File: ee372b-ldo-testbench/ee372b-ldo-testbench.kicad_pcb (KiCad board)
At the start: 4 copper layers, 100 x 100 mm, 128 parts, among them J1 PEC02SAAN, J10 OUT_S, J11 VOUT, J12 VDD_BUF, J13 V_SIG, J14 PEC03SAAN, J15 VSIG_BUF, J16 PEC03SAAN, J17 PEC03SAAN, J18 PEC03SAAN, J19 PEC03SAAN, J2 PEC02SAAN, J20 VREF_EXTERNAL, J21 PEC02SAAN, J22 PEC02SAAN, J23 PEC02SAAN, J24 PEC02SAAN, J25 PEC03SAAN, J3 GND, J4 1V8, J5 3v3_EXTERNAL, J6 GND, J9 IN_S, Q1 FDV305N, Q2 FDV305N, Q3 FDV305N, Q4 FDV305N, Q5 FDV305N, U1 MMSZ4679T1G, U3 ADS1220IPW, U4 BUF634AIDR

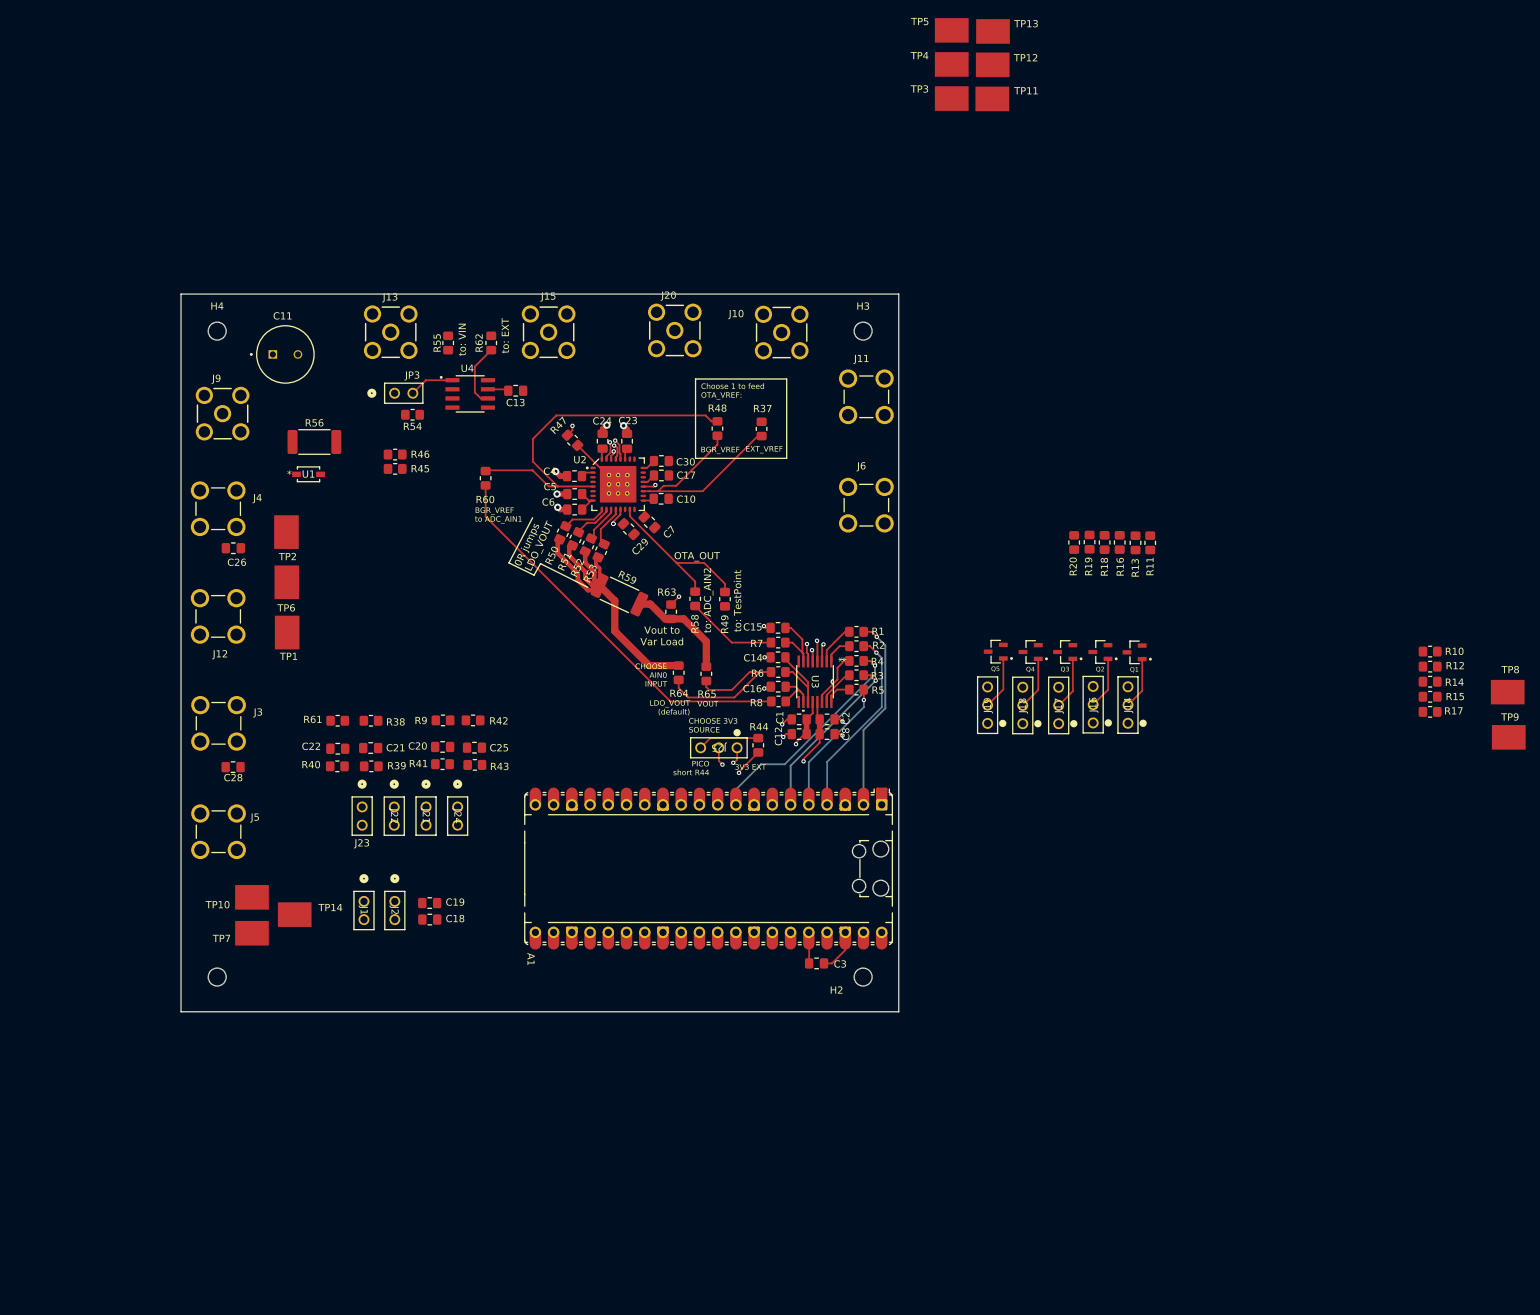
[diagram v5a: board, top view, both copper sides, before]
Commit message: resistor bank wired
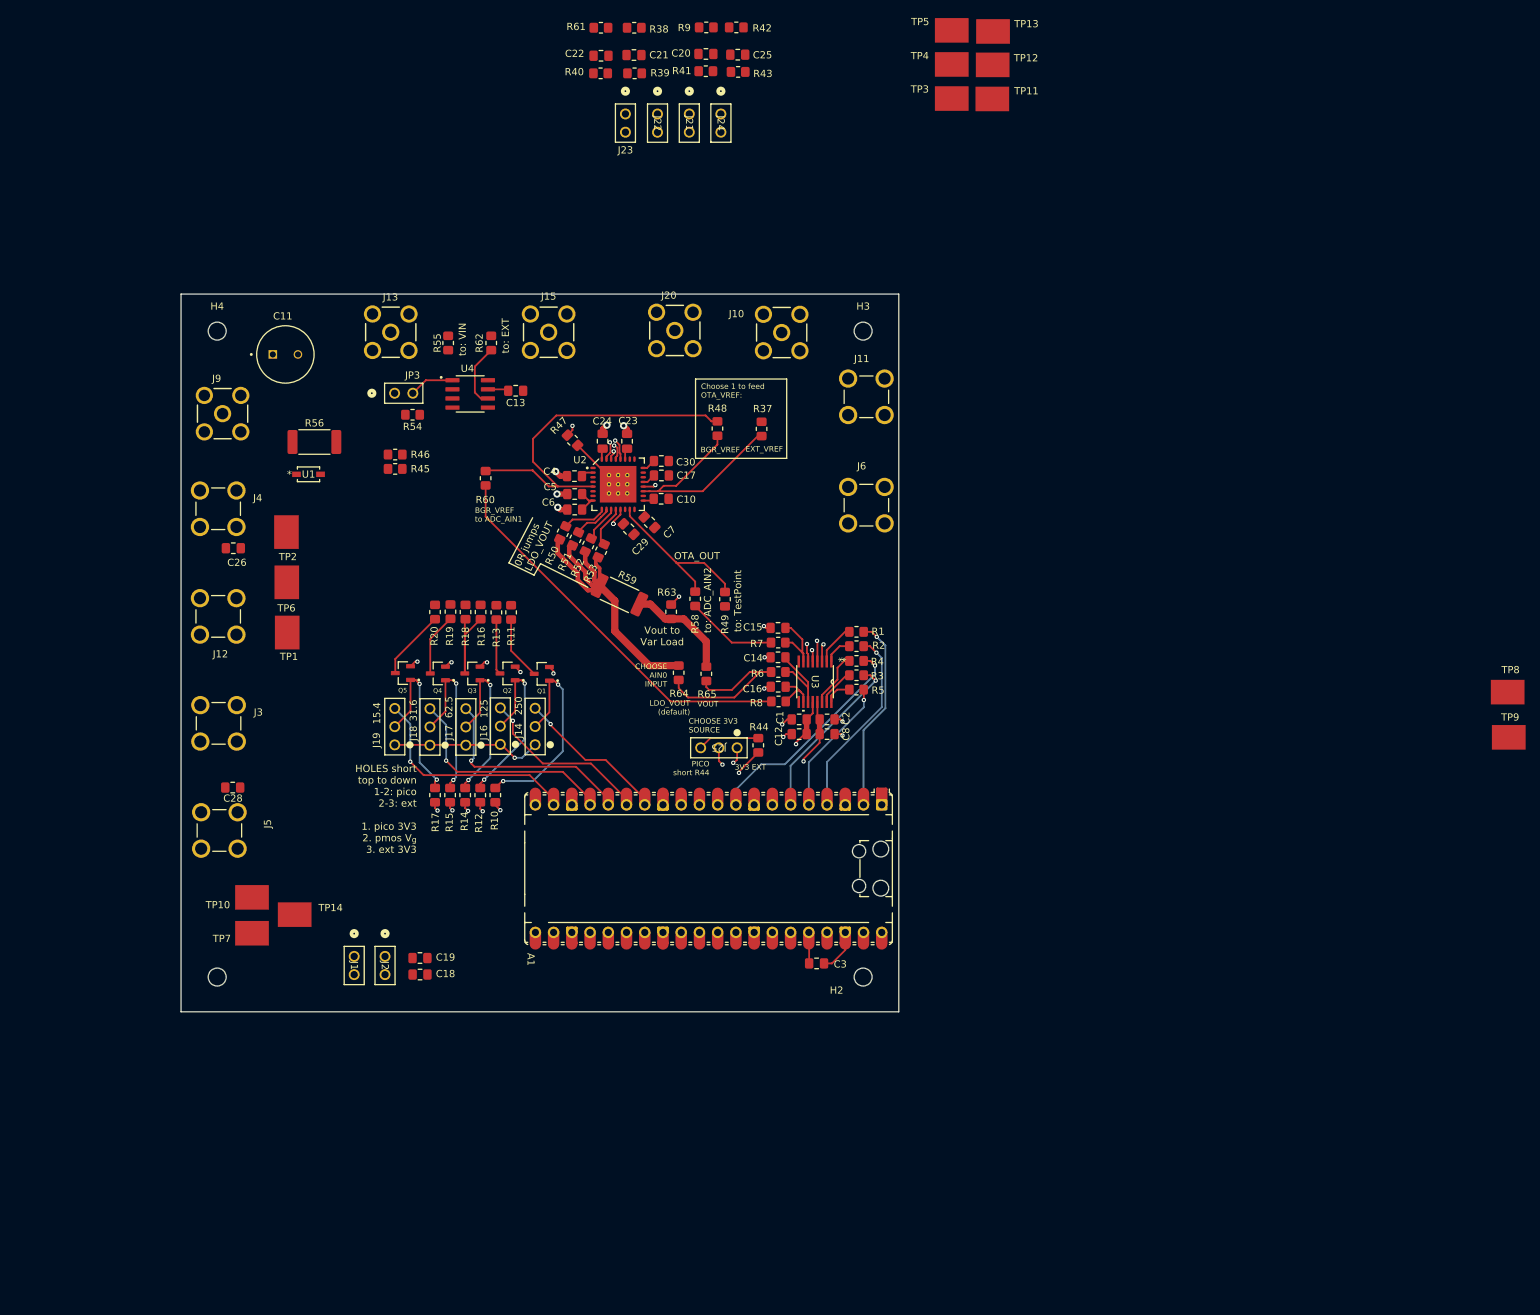
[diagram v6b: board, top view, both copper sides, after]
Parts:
- moved R17 139.1 mm to (175.3, 86.7), turned to -90 degrees
- moved R15 137.2 mm to (177.4, 86.7), turned to -90 degrees
- moved R14 135.4 mm to (179.6, 86.7), turned to -90 degrees
- moved R12 133.6 mm to (181.7, 86.7), turned to -90 degrees
- moved R10 131.8 mm to (183.8, 86.7), turned to -90 degrees
- moved C21 103.3 mm to (203.1, -16.5)
- moved C25 103.3 mm to (217.5, -16.5)
- moved R61 103.3 mm to (198.5, -20.3)
- moved C20 103.3 mm to (213.1, -16.6)
- moved J21 103.3 mm to (210.8, -8.26)
- moved J23 103.3 mm to (201.9, -8.26)
- moved J24 103.3 mm to (215.2, -8.26)
- moved R39 103.3 mm to (203.2, -13.9)
- moved R38 103.3 mm to (203.1, -20.3)
- moved R41 103.3 mm to (213.1, -14.2)
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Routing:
- net /pico_vg4: track 0.00 -> 30.5 mm, vias 0 -> 1
- net /pico_vg3: track 0.00 -> 30.4 mm, vias 0 -> 1
- net /pico_vg2: track 0.00 -> 29.4 mm, vias 0 -> 1
- net /pico_vg1: track 0.00 -> 23.9 mm, vias 0 -> 1
- net /VG0: track 7.21 -> 29.7 mm, vias 0 -> 2
- net /3V3: track 42.0 -> 63.0 mm, vias 3 -> 4
- net /pico_vg0: track 0.00 -> 20.7 mm, vias 0 -> 1
- net /VG1: track 7.25 -> 25.9 mm, vias 0 -> 2
- net /VG2: track 7.32 -> 24.8 mm, vias 0 -> 2
- net /VG4: track 7.42 -> 24.5 mm, vias 0 -> 2
- net /VG3: track 7.40 -> 24.0 mm, vias 0 -> 2
- net /VD2: track 0.00 -> 16.1 mm
- net GND: track 38.4 -> 50.9 mm, vias 23 -> 33
- net /VD4: track 0.00 -> 9.80 mm
- net /VD0: track 0.00 -> 8.89 mm
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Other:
- board text added: "125"
- board text added: "15.4"
- board text added: "250"
- board text added: "31.6"
- board text added: "62.5"
- board text added: "HOLES short top to down 1-2: pico 2-3: ext 1. pico 3V3 2. pmos V_{g} 3. ext 3V3"

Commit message: omg cleared DRC
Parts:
- added R57: 0, Resistor_SMD:R_0805_2012Metric_Pad1.20x1.40mm_HandSolder, F.Cu at (223.5, 113.0)
- moved TP8 127.3 mm to (197.5, 69.1)
- moved TP9 127.3 mm to (197.7, 77.0)
- moved TP11 121.3 mm to (155.7, 62.0)
- moved TP12 102.3 mm to (177.8, 54.2)
- moved TP4 101.5 mm to (207.2, 78.1)
- moved TP3 92.7 mm to (175.7, 48.4)
- moved TP13 76.0 mm to (196.5, 31.0)
- moved C22 66.3 mm to (215.8, 47.6)
- moved R61 66.3 mm to (215.8, 43.7)
- moved R40 66.3 mm to (215.8, 50.0)
- moved J21 66.3 mm to (232.0, 54.5)
- moved J22 66.3 mm to (227.5, 54.5)
- moved J24 66.3 mm to (236.4, 54.5)
- moved C21 66.1 mm to (220.4, 47.3)
- moved R38 66.1 mm to (220.4, 43.5)
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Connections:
- C28 pad 1: Net-(J5-Pin_1) -> /3V3_EXTERNAL
- J5 pad 1: Net-(J5-Pin_1) -> /3V3_EXTERNAL
- R46 pad 1: /LDO_GND -> /AIN3_LDO_GND
- TP10 pad 1: Net-(J5-Pin_1) -> /3V3_EXTERNAL
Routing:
- net Net-(A1-GND-Pad13): track 5.39 -> 147.7 mm
- net /VOUT: track 14.2 -> 132.0 mm, vias 0 -> 2
- net /LDO_VOUT: track 48.2 -> 154.2 mm, vias 0 -> 7
- net /3V3_EXTERNAL: track 2.27 -> 87.0 mm, vias 1 -> 0
- net GND: track 50.9 -> 125.0 mm, vias 33 -> 68
- net /1V8: track 0.00 -> 73.6 mm
- net /3V3_PICO: track 35.0 -> 105.9 mm
- net Net-(J4-Pin_1): track 0.00 -> 69.0 mm
- net /VARIABLE_LOAD: track 1.56 -> 59.0 mm, vias 1 -> 2
- net /VDD_BUF: track 2.91 -> 54.6 mm, vias 0 -> 1
- net /3V3: track 63.0 -> 114.2 mm, vias 4 -> 2
- net /c1_vin_jump: track 0.00 -> 50.6 mm
- net Net-(C10-Pad2): track 14.5 -> 62.4 mm, vias 0 -> 10
- net Net-(R49-Pad1): track 0.00 -> 38.4 mm, vias 0 -> 2
- net Net-(J24-Pad1): track 0.00 -> 27.5 mm, vias 0 -> 1
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- added copper zone on In2.Cu, net /1V8
- added copper zone on In2.Cu, net /3V3
- added copper zone on In2.Cu, net /3V3_EXTERNAL
- added copper zone on In2.Cu, net /3V3_PICO
- added copper zone on In2.Cu, net /LDO_VOUT
- added copper zone on In2.Cu, net /VDD_BUF
- added copper zone on In2.Cu, net /VOUT
- added copper zone on In2.Cu, net /VSIG
- added copper zone on In2.Cu, net Net-(C10-Pad2)
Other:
- board text added: "(not BUF)"
- board text added: "100nF 0.1uF"
- board text added: "10nF"
- board text added: "10uF"
- board text added: "1nF"
- board text added: "1uF"
- board text added: "3.3V"
- board text added: "3.3V EXT"
- board text added: "CONN VIN to LDO_VDD"
- board text added: "GND"
- board text added: "LDO VOUT"
- board text added: "VAR_RLOAD"
- board text added: "VIN 1.8V"
- board text added: "VIN_CAP"
- board text added: "VIN_S"
- board text added: "VOUT_LOAD"
- board text added: "VREF_EXT"
- board text added: "VSIG BUF"
- board text added: "VSIG BUF IN"
- board text added: "enable LDO_GND ADC AIN3"

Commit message: last sanity check DRC ERC
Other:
- board text added: "need to connect this shit so PICO GND is connected to LDO/GND"
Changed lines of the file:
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@@
+		)
+	)
+	(gr_text "need to connect this shit\nso PICO GND is connected\nto LDO/GND"
+		(at 220.6 113.3 0)
+		(layer "F.SilkS")
+		(effects
+			(font
+				(size 0.762 0.762)
+				(thickness 0.15)
+			)
+			(justify right)
 		)
 	)
